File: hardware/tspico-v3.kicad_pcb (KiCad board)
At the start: 4 copper layers, 130 x 64 mm, 157 parts, among them J1 USB-C, J2 microSD, J3 OLED 1.27in 128x96, J4 3.5mm stereo, J5 Joystick, P1 TS2068_Edge, SW1 TS Reset, SW2 NMI, SW3 RUN, SW4 BOOTSEL, U1 74LVC245APW, U10 74LVC257APW, U11 74LVC257APW, U12 74LVC574APW, U13 74LVC574APW, U14 74HC273PW, U15 74LVC541APW, U16 74LVC139PW, U2 74LVC245APW, U20 RP2350B, U21 W25Q128JVSIQ, U22 APS6404L-3SQR-SN, U3 74LVC245APW, U30 TLV1117LV33, U31 TLV1117LV33, U4 74LVC245APW, U40 ESP32-C3-WROOM-02-N4, U5 74LVC04APW, U50 MCP6002, U6 74LVC08APW, U7 74LVC06APW, U8 74LVC126APW, U9 74LVC1G86, Y1 12MHz

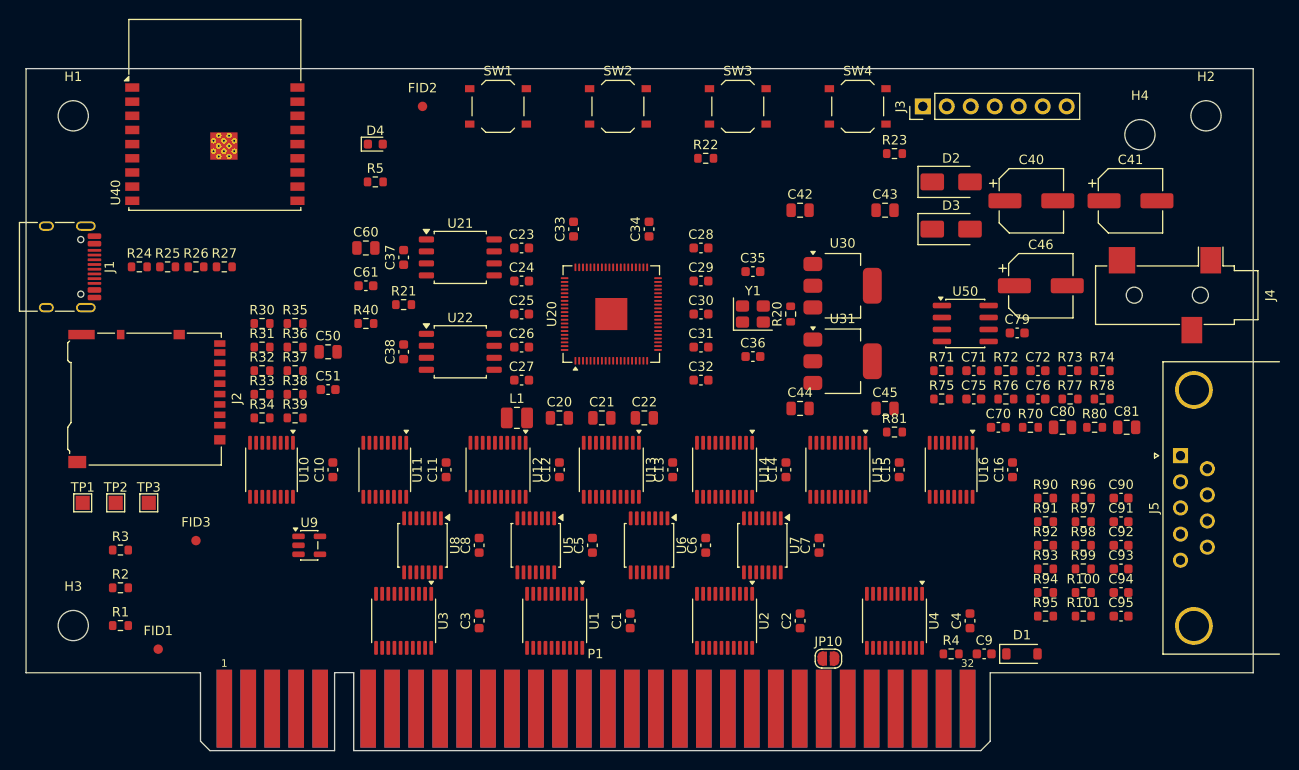
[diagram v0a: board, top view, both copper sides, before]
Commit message: Autoroute on the reordered 72 mm board: 521/532 routed (headless Freerouting)
Co-Authored-By: Claude Fable 5.1 <noreply@anthropic.com>
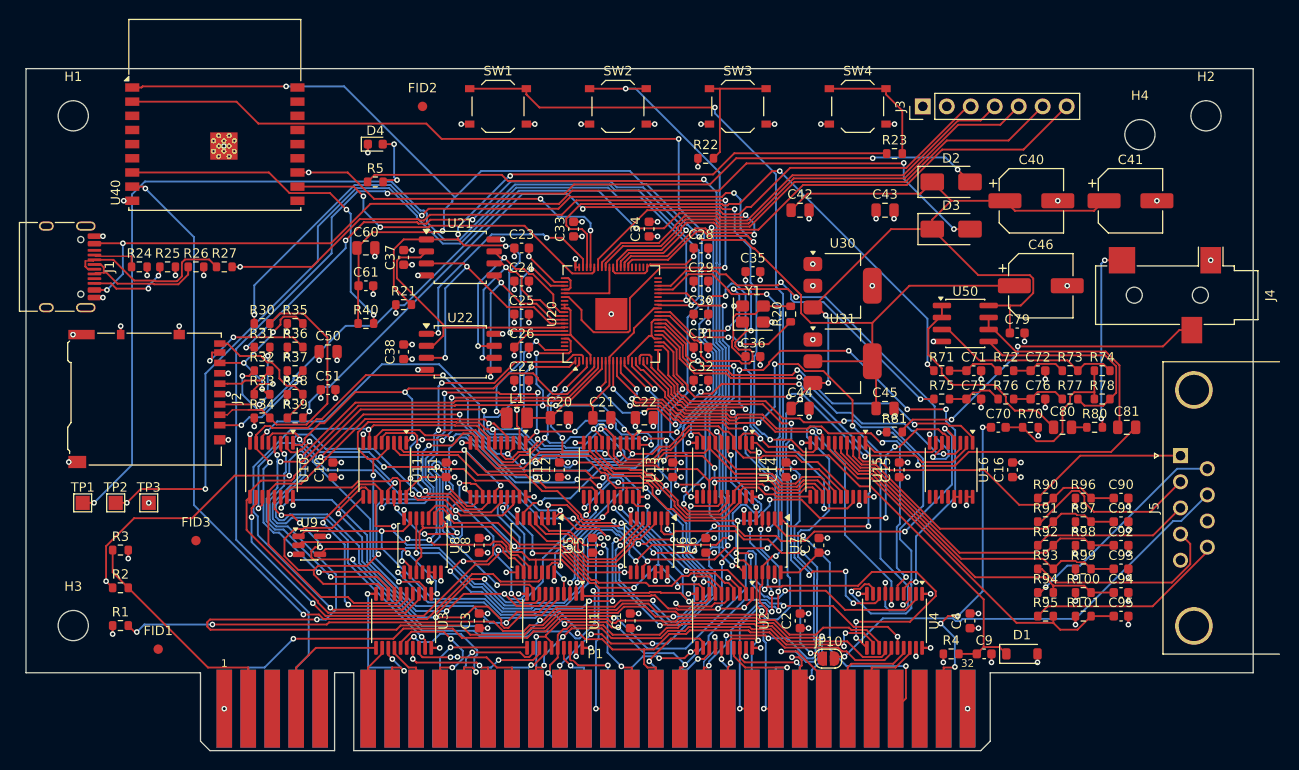
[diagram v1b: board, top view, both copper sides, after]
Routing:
- net +3V3_WIFI: track 0.00 -> 146.6 mm, vias 0 -> 3
- net MD0: track 0.00 -> 144.9 mm, vias 0 -> 14
- net MD3: track 0.00 -> 139.3 mm, vias 0 -> 4
- net +5V_EDGE: track 0.00 -> 131.5 mm, vias 0 -> 3
- net TAPE_OUT: track 0.00 -> 126.6 mm, vias 0 -> 5
- net +5V: track 0.00 -> 123.2 mm, vias 0 -> 4
- net MD6: track 0.00 -> 122.7 mm, vias 0 -> 10
- net GND: track 0.00 -> 121.3 mm, vias 0 -> 117
- net RESET_HOLD: track 0.00 -> 120.0 mm, vias 0 -> 4
- net MD5: track 0.00 -> 116.6 mm, vias 0 -> 10
- net /RP2350B Core/SWCLK: track 0.00 -> 114.2 mm, vias 0 -> 2
- net MD7: track 0.00 -> 111.6 mm, vias 0 -> 4
- net MA8: track 0.00 -> 110.2 mm, vias 0 -> 5
- net +3V3: track 0.00 -> 109.5 mm, vias 0 -> 69
- net MD1: track 0.00 -> 107.8 mm, vias 0 -> 5
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
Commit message: Route: 520/532 on the 72 mm board, zero DRC violations; keepout limited to the chip body
Co-Authored-By: Claude Fable 5.1 <noreply@anthropic.com>
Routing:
- net Z80_A15: track 67.0 -> 57.2 mm
- net GND: track 121.3 -> 125.7 mm

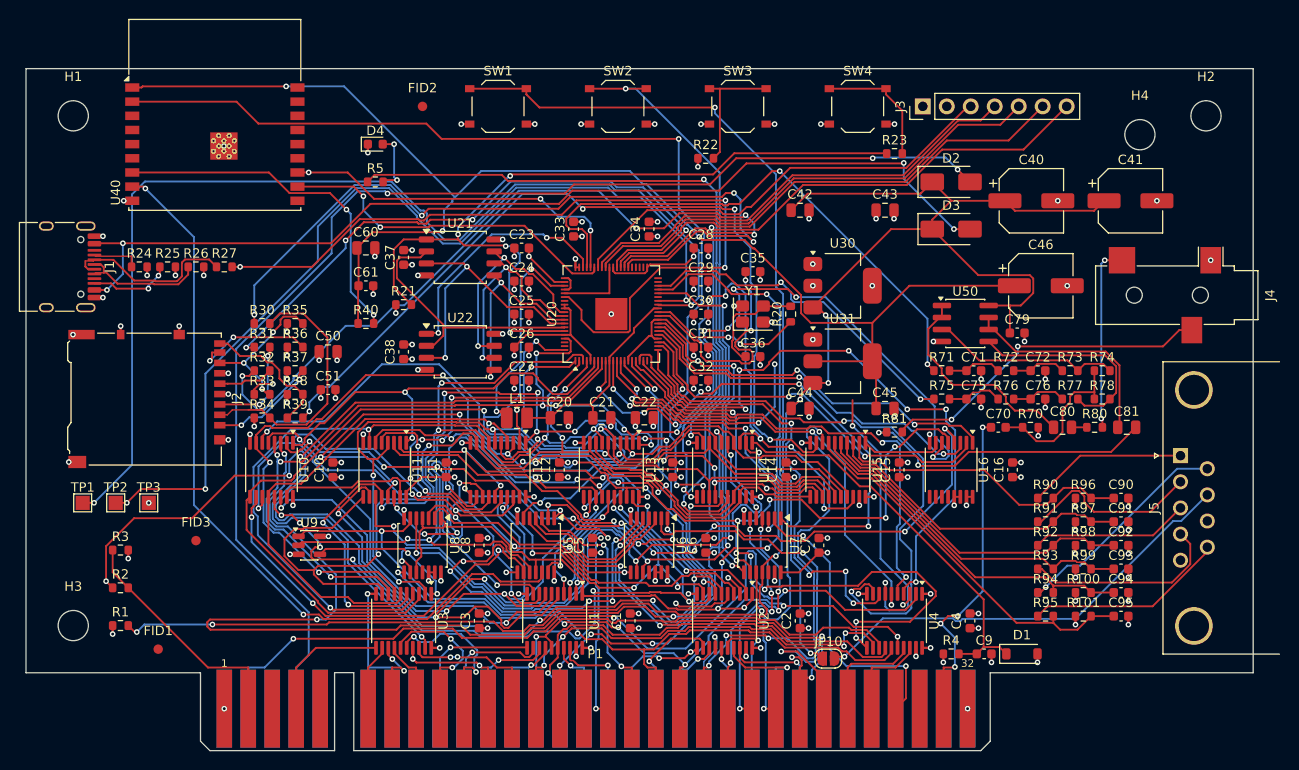
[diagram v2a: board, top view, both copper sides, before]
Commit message: Layout: SD socket flush with the edge, flash/PSRAM 2 mm further from U20, thinner left decoupling column
Co-Authored-By: Claude Fable 5.1 <noreply@anthropic.com>
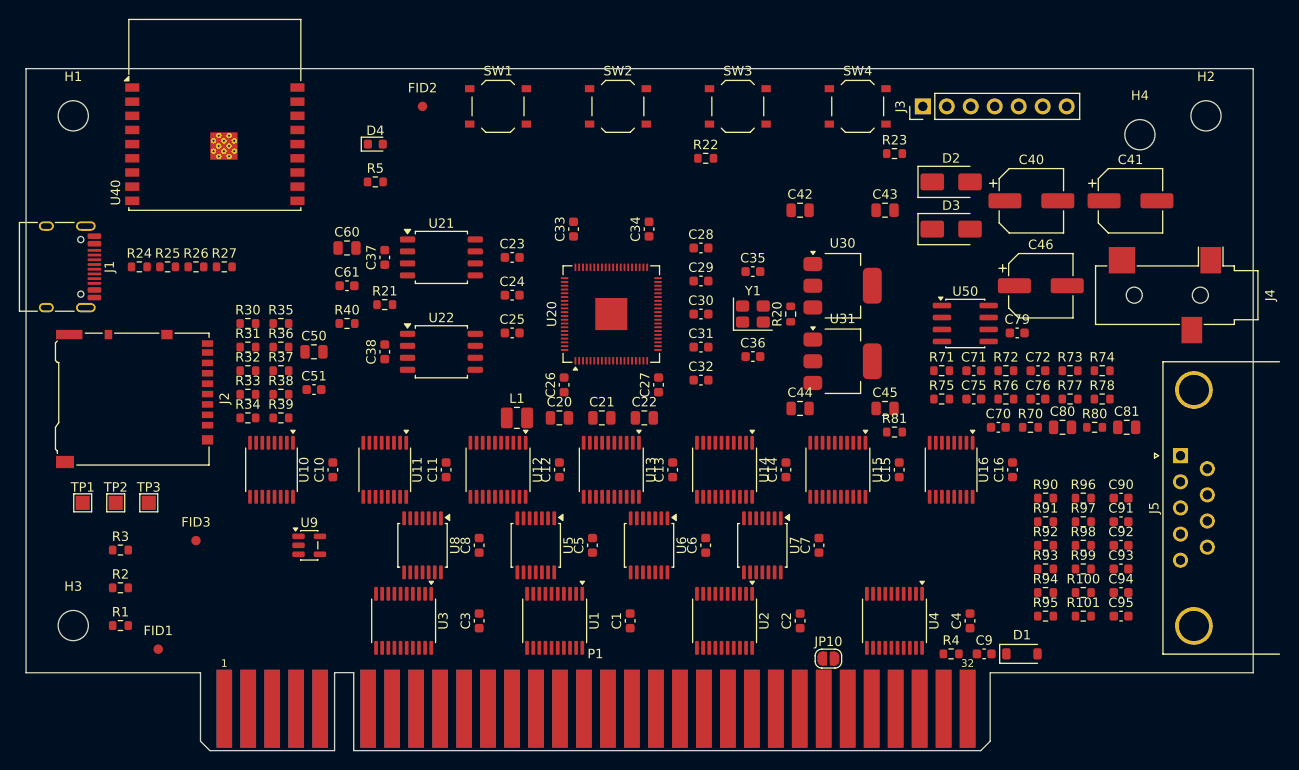
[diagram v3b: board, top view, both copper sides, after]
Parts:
- moved C27 14.5 mm to (67.0, 33.5), turned to 90 degrees
- moved C26 6.02 mm to (57.0, 33.5), turned to 90 degrees
- moved C25 2.24 mm to (51.5, 28.0)
- moved C37 2.00 mm to (38.0, 20.0)
- moved C38 2.00 mm to (38.0, 30.0)
- moved C60 2.00 mm to (34.0, 19.0)
- moved C61 2.00 mm to (34.0, 23.0)
- moved R21 2.00 mm to (38.0, 25.0)
- moved R40 2.00 mm to (34.0, 27.0)
- moved U21 2.00 mm to (44.0, 20.0)
- moved U22 2.00 mm to (44.0, 30.0)
- moved C24 1.80 mm to (51.5, 24.0)
- moved C50 1.50 mm to (30.5, 30.0)
- moved C51 1.50 mm to (30.5, 34.0)
- moved R30 1.50 mm to (23.5, 27.0)
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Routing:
- net +3V3_WIFI: track 146.6 -> 0.00 mm, vias 3 -> 0
- net MD0: track 144.9 -> 0.00 mm, vias 14 -> 0
- net MD3: track 139.3 -> 0.00 mm, vias 4 -> 0
- net +5V_EDGE: track 131.5 -> 0.00 mm, vias 3 -> 0
- net TAPE_OUT: track 126.6 -> 0.00 mm, vias 5 -> 0
- net GND: track 125.7 -> 0.00 mm, vias 117 -> 0
- net +5V: track 123.2 -> 0.00 mm, vias 4 -> 0
- net MD6: track 122.7 -> 0.00 mm, vias 10 -> 0
- net RESET_HOLD: track 120.0 -> 0.00 mm, vias 4 -> 0
- net MD5: track 116.6 -> 0.00 mm, vias 10 -> 0
- net /RP2350B Core/SWCLK: track 114.2 -> 0.00 mm, vias 2 -> 0
- net MD7: track 111.6 -> 0.00 mm, vias 4 -> 0
- net MA8: track 110.2 -> 0.00 mm, vias 5 -> 0
- net +3V3: track 109.5 -> 0.00 mm, vias 69 -> 0
- net MD1: track 107.8 -> 0.00 mm, vias 5 -> 0
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
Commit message: Route: 525/532 on the 72 mm board after SD/flash/decoupling moves, zero DRC violations
Co-Authored-By: Claude Fable 5.1 <noreply@anthropic.com>
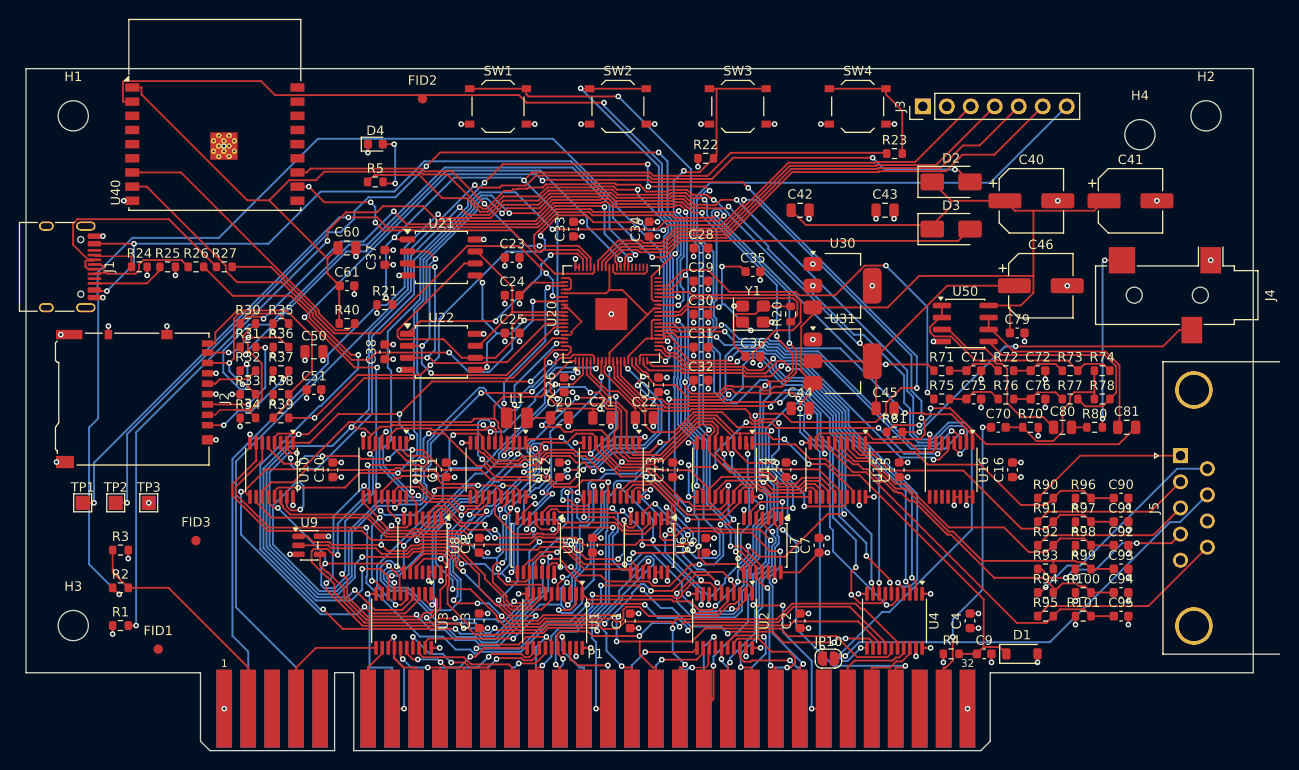
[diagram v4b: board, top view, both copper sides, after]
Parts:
- moved FID2 0.80 mm to (42.0, 3.20)
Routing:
- net MD5: track 0.00 -> 193.0 mm, vias 0 -> 10
- net MA7: track 0.00 -> 173.3 mm, vias 0 -> 10
- net /2068 Interface/SPKR_TAPE: track 0.00 -> 170.5 mm, vias 0 -> 3
- net MA10: track 0.00 -> 165.3 mm, vias 0 -> 8
- net MA8: track 0.00 -> 160.6 mm, vias 0 -> 8
- net MD2: track 0.00 -> 155.2 mm, vias 0 -> 6
- net nMRD: track 0.00 -> 146.5 mm, vias 0 -> 9
- net +3V3_WIFI: track 0.00 -> 143.5 mm, vias 0 -> 2
- net MD0: track 0.00 -> 142.0 mm, vias 0 -> 9
- net RESET_HOLD: track 0.00 -> 138.3 mm, vias 0 -> 5
- net +5V_EDGE: track 0.00 -> 123.8 mm, vias 0 -> 3
- net GND: track 0.00 -> 121.9 mm, vias 0 -> 117
- net +5V: track 0.00 -> 121.7 mm, vias 0 -> 2
- net MD3: track 0.00 -> 120.2 mm, vias 0 -> 2
- net TAPE_OUT: track 0.00 -> 118.5 mm, vias 0 -> 2
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
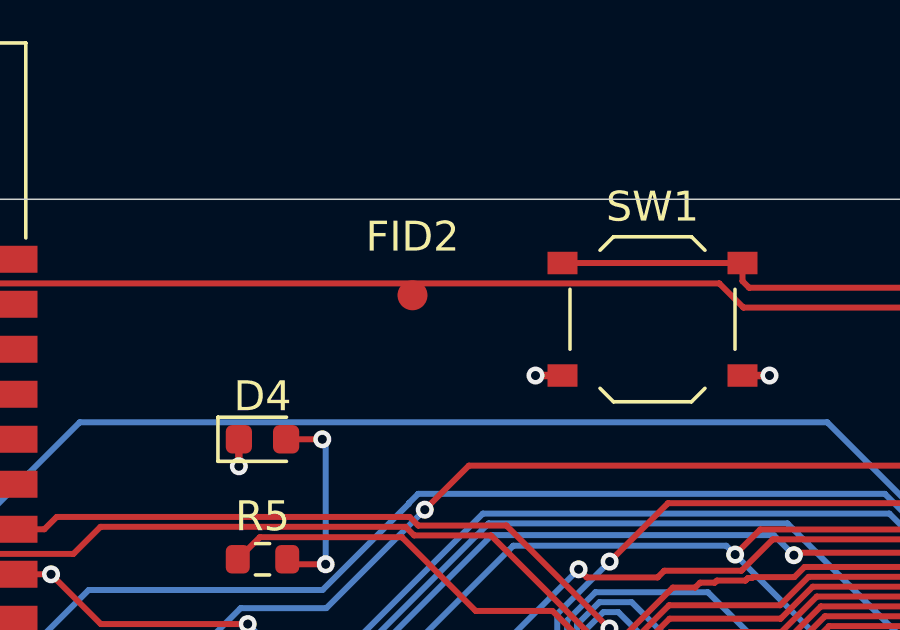
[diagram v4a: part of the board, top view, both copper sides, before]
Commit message: Move FID2 clear of the WIFI_EN track
Co-Authored-By: Claude Fable 5.1 <noreply@anthropic.com>
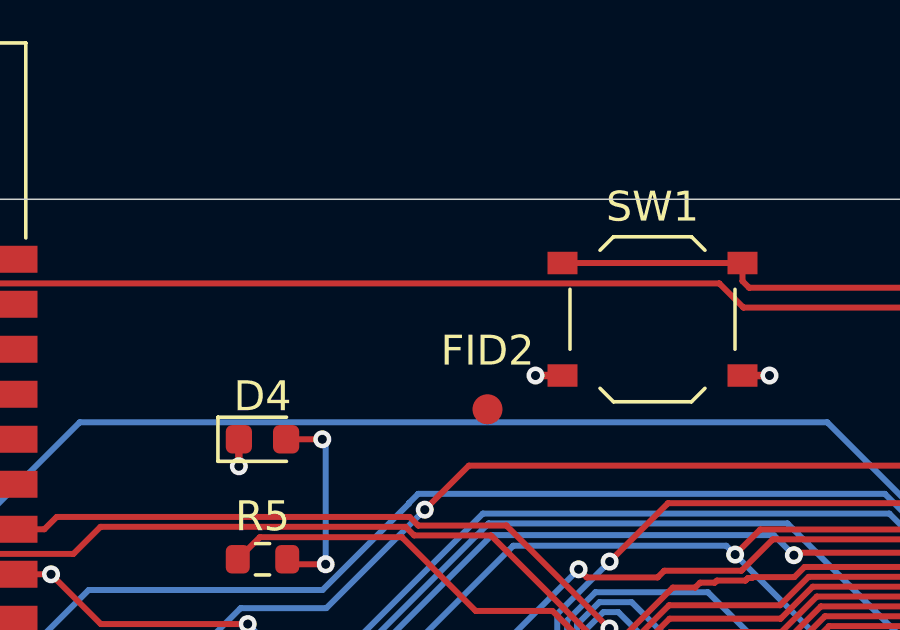
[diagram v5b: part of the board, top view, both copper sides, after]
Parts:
- moved FID2 4.55 mm to (44.5, 7.00)
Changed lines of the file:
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@@
 	(footprint "Fiducial:Fiducial_1mm_Mask2mm"
 		(layer "F.Cu")
-		(at 42 3.2)
+		(at 44.5 7)
 		(descr "Fiducial, circular marking, 1mm bare copper, 2mm soldermask opening (Level A)")
 		(tags "fiducial")

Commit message: SD socket shell 0.35 mm from the edge (copper-to-edge rule), SD nets rerouted: 524/532, zero DRC violations
Co-Authored-By: Claude Fable 5.1 <noreply@anthropic.com>
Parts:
- moved J2 2.75 mm to (8.75, 35.0)
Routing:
- net SD_CD: track 109.4 -> 174.4 mm, vias 7 -> 14
- net /SD and Display/SD_MOSI_J: track 12.1 -> 16.6 mm
- net /SD and Display/SD_DAT2: track 11.2 -> 14.2 mm
- net /SD and Display/SD_CS_J: track 16.9 -> 19.7 mm
- net /SD and Display/SD_SCK_J: track 5.67 -> 8.42 mm
- net /SD and Display/SD_DAT1: track 9.68 -> 12.4 mm
- net GND: track 121.9 -> 123.8 mm, vias 117 -> 116
- net /SD and Display/SD_MISO_J: track 18.3 -> 18.6 mm, vias 2 -> 3
